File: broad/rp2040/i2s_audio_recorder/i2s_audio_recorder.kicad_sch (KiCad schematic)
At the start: 53 parts, among them J1 USB_C_Receptacle_USB2.0_16P, J2 Conn_01x04_Pin, J3 SD_Card_Device, J4 Conn_01x08_Pin, J5 Conn_01x08_Pin, J6 Conn_01x08_Pin, SW1 TS-1101-C-W, SW2 TS-1101-C-W, SW3 TS-1101-C-W, SW4 TS-1101-C-W, U1 MSM261S4030H0R, U1 SMBJ5.0CA, U2 RP2040, U3 SMBJ5.0CA, U4 SMBJ5.0CA, U5 AMS1117-3.3, U7 W25Q128JVS, Y1 12M

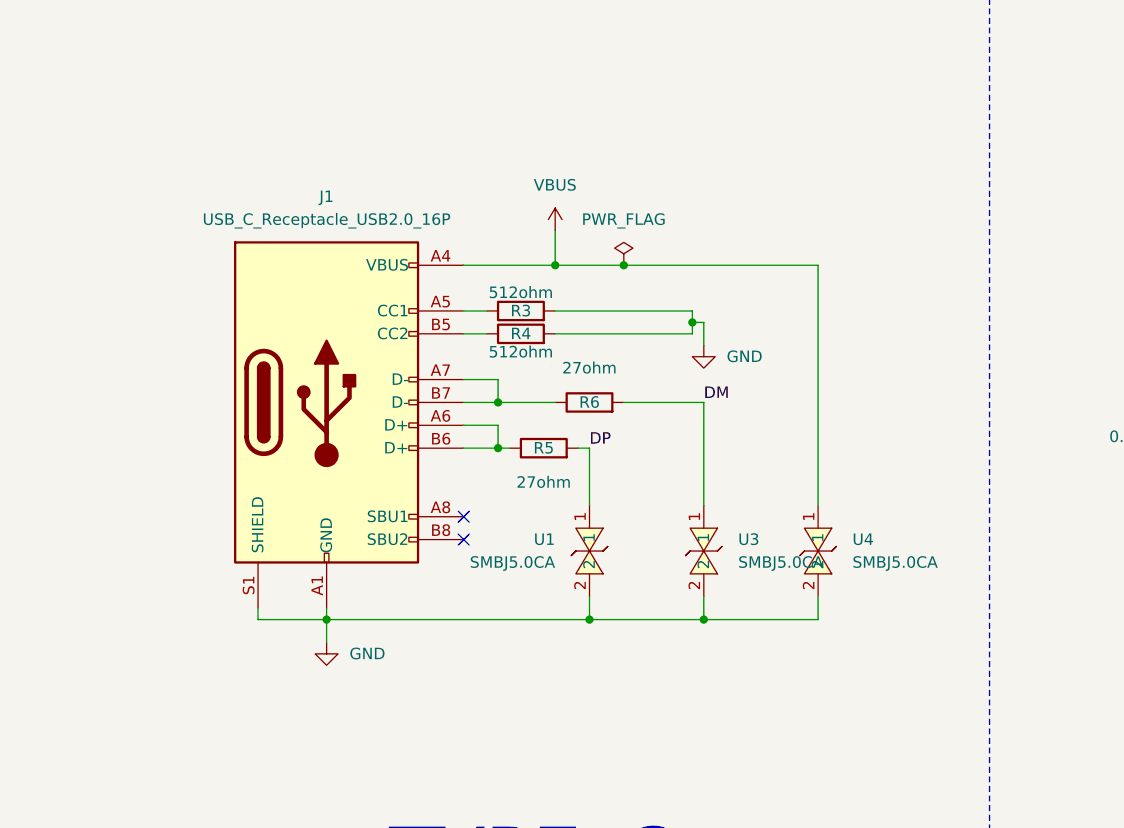
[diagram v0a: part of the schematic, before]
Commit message: Add power supplier LED for `i2d_audio_recorder`
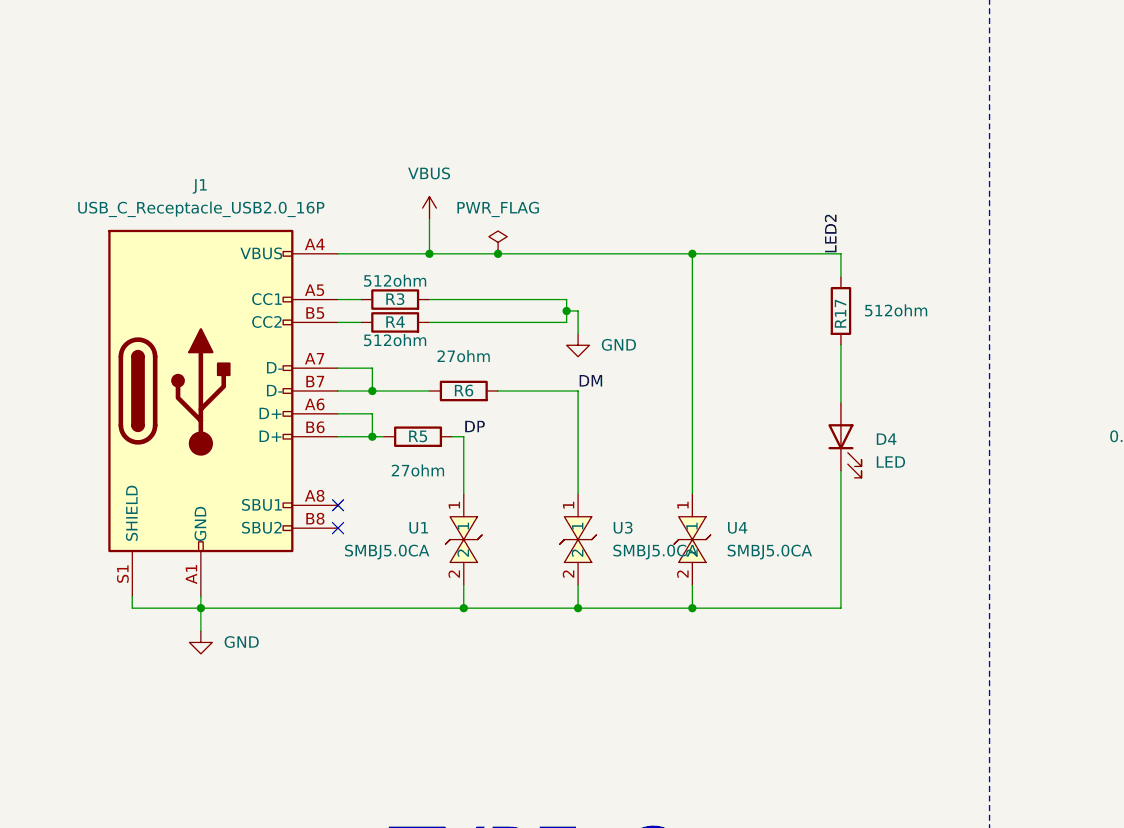
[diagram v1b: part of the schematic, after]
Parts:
- added D4: LED, Capacitor_SMD:C_0603_1608Metric, symbol Device:LED
- added R17: 512ohm, Resistor_SMD:R_0603_1608Metric, symbol Device:R
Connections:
- net LED2 is gone; now on net VBUS: R9.1, U2.31 (GPIO20)
- net GND: now also D4.1 (K)
- net VBUS: now also R17.1
- new net: D4.2 (A), R17.2
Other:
- moved on the sheet: J1, R3, R4, R5, R6, U1, U3, U4

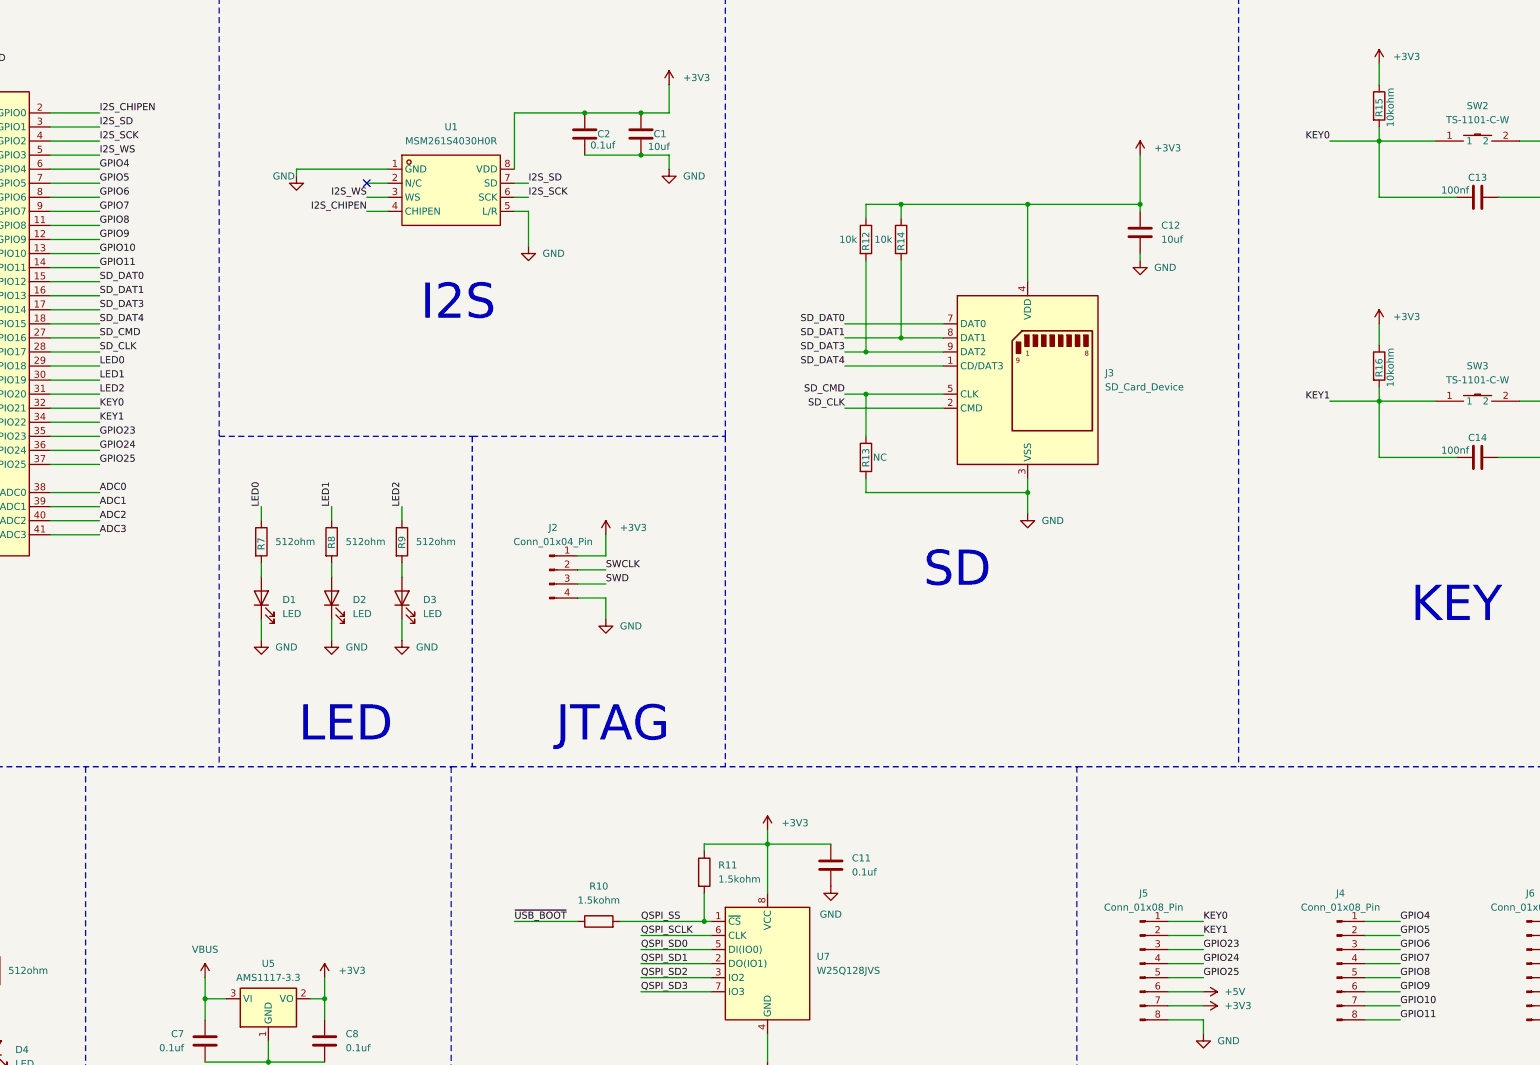
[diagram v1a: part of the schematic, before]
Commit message: Move **I2S_AUDIO** from `GPIO0`~`GPIO3` to `GPIO4`~`GPIO7`
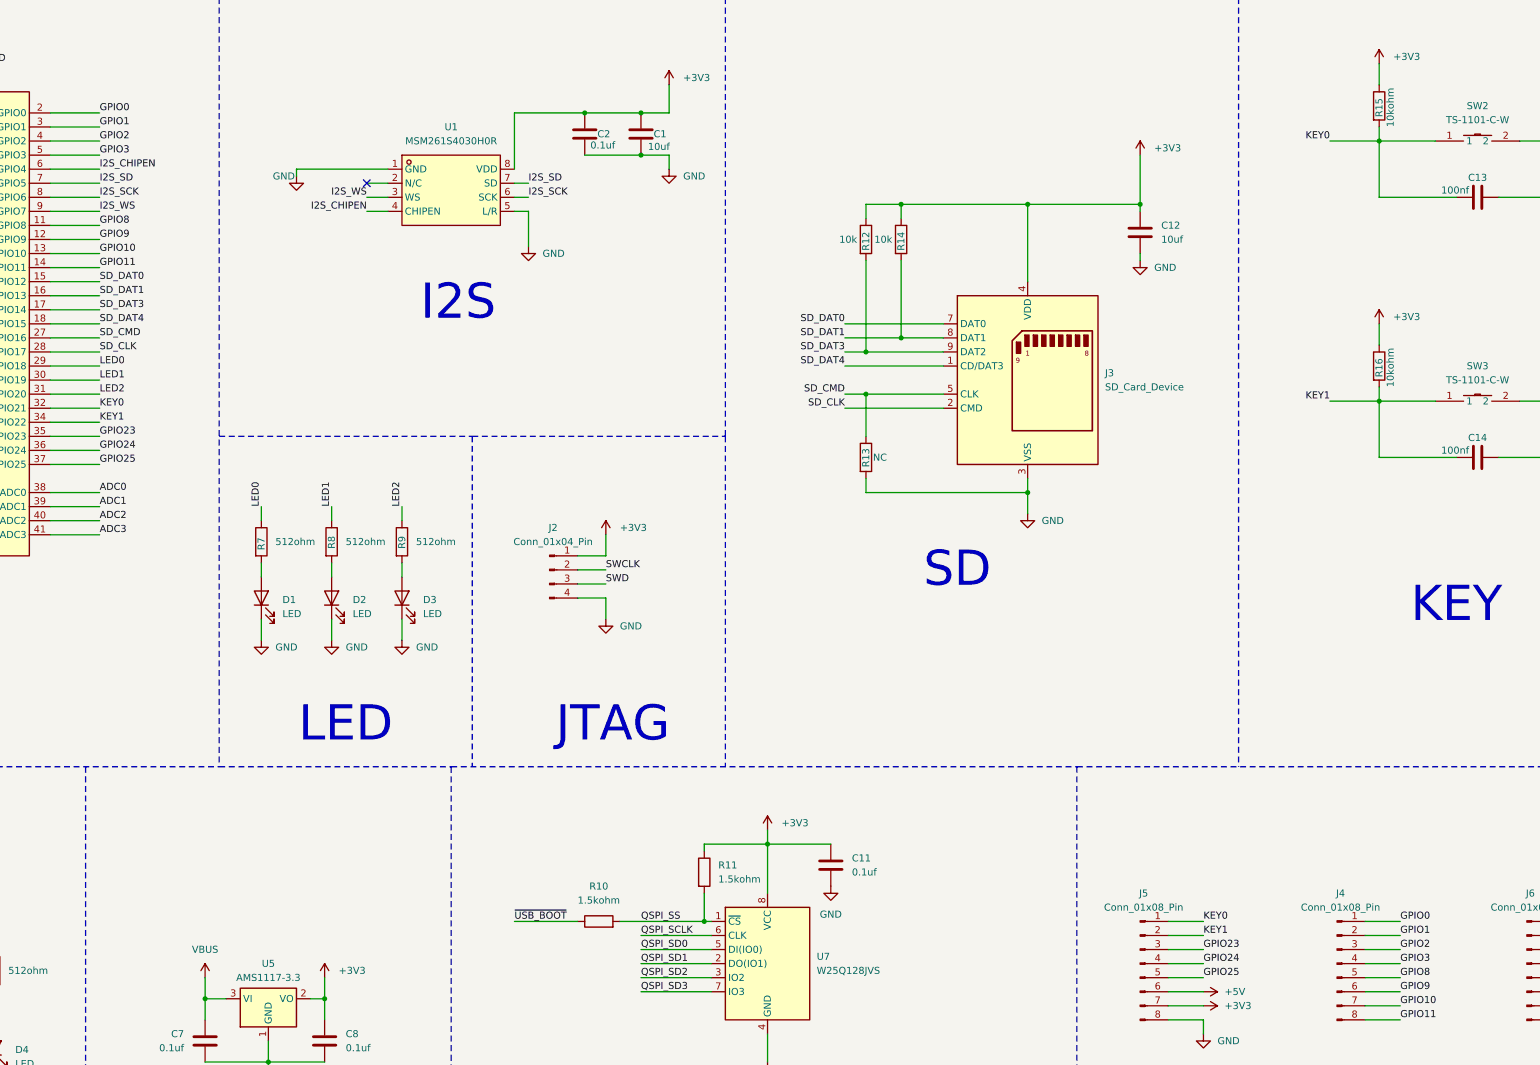
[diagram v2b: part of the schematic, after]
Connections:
- net I2S_CHIPEN: now also U2.6 (GPIO4); no longer U2.2 (GPIO0)
- net I2S_SCK: now also U2.8 (GPIO6); no longer U2.4 (GPIO2)
- net I2S_SD: now also U2.7 (GPIO5); no longer U2.3 (GPIO1)
- net I2S_WS: now also U2.9 (GPIO7); no longer U2.5 (GPIO3)
- net GPIO4 renamed GPIO0
- net GPIO0: now also U2.2 (GPIO0); no longer U2.6 (GPIO4)
- net GPIO5 renamed GPIO1
- net GPIO1: now also U2.3 (GPIO1); no longer U2.7 (GPIO5)
- net GPIO6 renamed GPIO2
- net GPIO2: now also U2.4 (GPIO2); no longer U2.8 (GPIO6)
- net GPIO7 renamed GPIO3
- net GPIO3: now also U2.5 (GPIO3); no longer U2.9 (GPIO7)
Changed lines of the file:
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@@
-		)
-	)
-	(label "I2S_CHIPEN"
-		(at 123.19 50.8 0)
-		(fields_autoplaced yes)
-		(effects
-			(font
-				(size 1.27 1.27)
-			)
-			(justify left bottom)
 		)
 	)
@@
 		)
 	)
-	(label "GPIO6"
-		(at 123.19 66.04 0)
-		(fields_autoplaced yes)
-		(effects
-			(font
-				(size 1.27 1.27)
-			)
-			(justify left bottom)
-		)
-	)
-	(label "GPIO4"
-		(at 123.19 60.96 0)
-		(fields_autoplaced yes)
-		(effects
-			(font
-				(size 1.27 1.27)
-			)
-			(justify left bottom)
-		)
-	)
 	(label "ADC_VERF"
 		(at 393.7 209.55 0)
@@
 		)
 	)
+	(label "I2S_CHIPEN"
+		(at 123.19 60.96 0)
+		(fields_autoplaced yes)
+		(effects
+			(font
+				(size 1.27 1.27)
+			)
+			(justify left bottom)
+		)
+	)
 	(label "KEY1"
 		(at 123.19 106.68 0)
@@
 		)
 	)
+	(label "I2S_SCK"
+		(at 123.19 66.04 0)
+		(fields_autoplaced yes)
+		(effects
+			(font
+				(size 1.27 1.27)
+			)
+			(justify left bottom)
+		)
+	)
 	(label "QSPI_SD1"
 		(at 220.98 204.47 0)
@@
 		)
 	)
-	(label "GPIO7"
-		(at 123.19 68.58 0)
+	(label "GPIO1"
+		(at 123.19 53.34 0)
 		(fields_autoplaced yes)
 		(effects
@@
 		)
 	)
-	(label "I2S_SD"
-		(at 123.19 53.34 0)
-		(fields_autoplaced yes)
-		(effects
-			(font
-				(size 1.27 1.27)
-			)
-			(justify left bottom)
-		)
-	)
 	(label "ADC3"
 		(at 393.7 204.47 0)
@@
 		)
 	)
-	(label "GPIO4"
+	(label "GPIO0"
 		(at 358.14 196.85 0)
 		(fields_autoplaced yes)
@@
 		)
 	)
-	(label "GPIO5"
+	(label "GPIO1"
 		(at 358.14 199.39 0)
 		(fields_autoplaced yes)
@@
 		)
 	)
-	(label "GPIO7"
+	(label "GPIO3"
 		(at 358.14 204.47 0)
 		(fields_autoplaced yes)
@@
 		)
 	)
-	(label "I2S_SCK"
-		(at 123.19 55.88 0)
+	(label "GPIO0"
+		(at 123.19 50.8 0)
 		(fields_autoplaced yes)
 		(effects
@@
 		)
 	)
-	(label "GPIO5"
-		(at 123.19 63.5 0)
+	(label "GPIO3"
+		(at 123.19 58.42 0)
 		(fields_autoplaced yes)
 		(effects
@@
 		)
 	)
-	(label "GPIO6"
+	(label "GPIO2"
+		(at 123.19 55.88 0)
+		(fields_autoplaced yes)
+		(effects
+			(font
+				(size 1.27 1.27)
+			)
+			(justify left bottom)
+		)
+	)
+	(label "GPIO2"
 		(at 358.14 201.93 0)
 		(fields_autoplaced yes)
@@
 	)
 	(label "I2S_WS"
-		(at 123.19 58.42 0)
+		(at 123.19 68.58 0)
 		(fields_autoplaced yes)
 		(effects
@@
 		(fields_autoplaced yes)
 		(effects
+			(font
+				(size 1.27 1.27)
+			)
+			(justify left bottom)
+		)
+	)
+	(label "I2S_SD"
+		(at 123.19 63.5 0)
+		(fields_autoplaced yes)
+		(effects
